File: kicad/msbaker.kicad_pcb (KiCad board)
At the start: 4 copper layers, 14 x 62 mm, 41 parts, among them J1 USB_B_Micro, J2 Micro_SD_Card, J3 GPIO, M2 MountingHole_2.2mm_M2_ISO1458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, U1 MIC5365-3.3YC5, U2 W25Q128JVS, U3 RP2040, U4 LSM6DSO32, Y1 12MHz

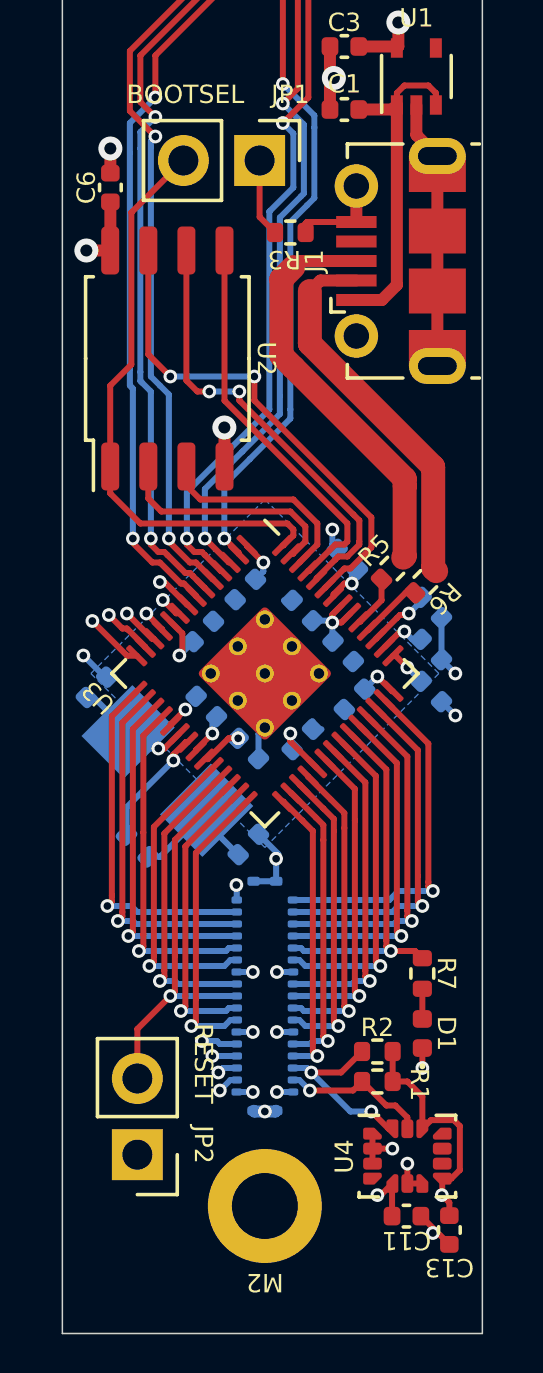
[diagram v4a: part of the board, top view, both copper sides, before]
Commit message: Added M2 screw holes to the solder paste layer to give points to align the solder paste stencil
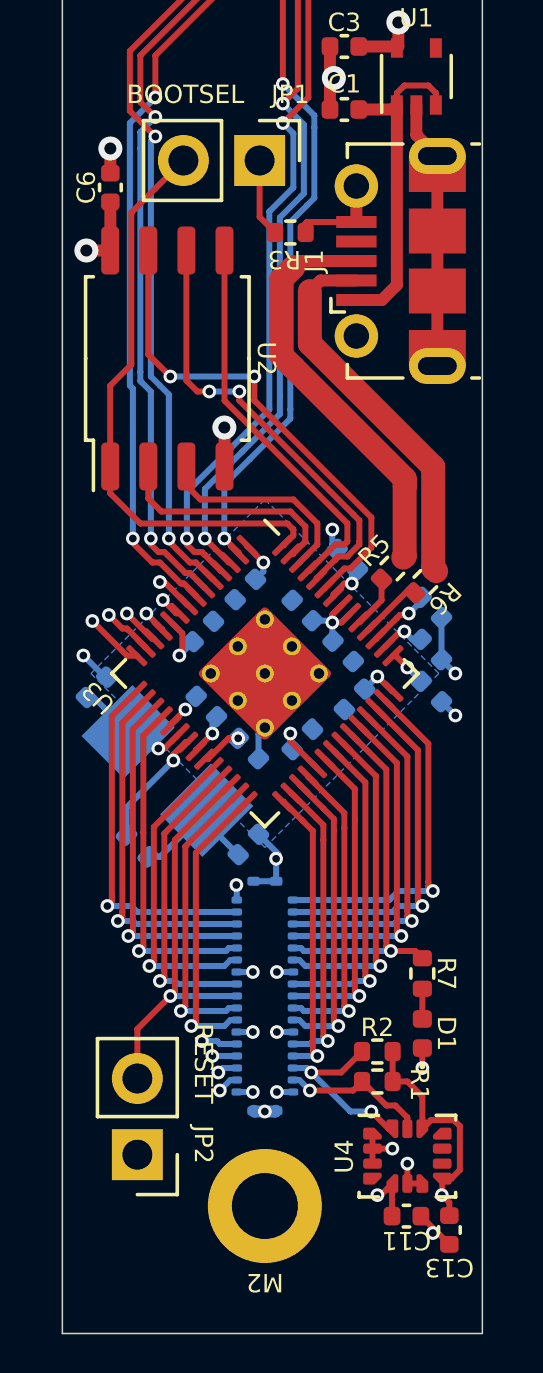
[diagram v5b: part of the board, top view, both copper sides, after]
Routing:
- net GND: track 38.5 -> 37.4 mm
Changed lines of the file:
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@@
       (outputformat 1)
       (mirror false)
-      (drillshape 1)
+      (drillshape 0)
       (scaleselection 1)
-      (outputdirectory "")
+      (outputdirectory "gerbers/")
     )
   )
@@
           ) (width 0.15) (fill yes))
       ))
-    (pad "2" smd roundrect (at -1.1625 -0.25) (size 0.625 0.4) (layers "F.Cu" "F.Paste" "F.Mask") (roundrect_rratio 0.25)
+    (pad "2" smd roundrect (at -1.1625 -0.25) (size 0.625 0.34) (layers "F.Cu" "F.Paste" "F.Mask") (roundrect_rratio 0.25)
       (net 2 "GND") (pinfunction "SDX") (pintype "bidirectional"))
-    (pad "3" smd roundrect (at -1.1625 0.25) (size 0.625 0.4) (layers "F.Cu" "F.Paste" "F.Mask") (roundrect_rratio 0.25)
+    (pad "3" smd roundrect (at -1.1625 0.25) (size 0.625 0.34) (layers "F.Cu" "F.Paste" "F.Mask") (roundrect_rratio 0.25)
       (net 2 "GND") (pinfunction "SCX") (pintype "input"))
     (pad "4" smd custom (at -1.1625 0.75) (size 0.223223 0.223223) (layers "F.Cu" "F.Paste" "F.Mask")
@@
           ) (width 0.15) (fill yes))
       ))
-    (pad "6" smd roundrect (at 0 0.9125) (size 0.4 0.625) (layers "F.Cu" "F.Paste" "F.Mask") (roundrect_rratio 0.25)
+    (pad "6" smd roundrect (at 0 0.9125) (size 0.34 0.625) (layers "F.Cu" "F.Paste" "F.Mask") (roundrect_rratio 0.25)
       (net 2 "GND") (pinfunction "GND") (pintype "power_in"))
     (pad "7" smd custom (at 0.5 0.9125) (size 0.223223 0.223223) (layers "F.Cu" "F.Paste" "F.Mask")
@@
           ) (width 0.15) (fill yes))
       ))
-    (pad "9" smd roundrect (at 1.1625 0.25) (size 0.625 0.4) (layers "F.Cu" "F.Paste" "F.Mask") (roundrect_rratio 0.25)
+    (pad "9" smd roundrect (at 1.1625 0.25) (size 0.625 0.34) (layers "F.Cu" "F.Paste" "F.Mask") (roundrect_rratio 0.25)
       (net 56 "unconnected-(U4-Pad9)") (pinfunction "INT2") (pintype "output+no_connect"))
-    (pad "10" smd roundrect (at 1.1625 -0.25) (size 0.625 0.4) (layers "F.Cu" "F.Paste" "F.Mask") (roundrect_rratio 0.25)
+    (pad "10" smd roundrect (at 1.1625 -0.25) (size 0.625 0.34) (layers "F.Cu" "F.Paste" "F.Mask") (roundrect_rratio 0.25)
       (net 57 "unconnected-(U4-Pad10)") (pinfunction "NC") (pintype "no_connect"))
     (pad "11" smd custom (at 1.1625 -0.75) (size 0.223223 0.223223) (layers "F.Cu" "F.Paste" "F.Mask")
@@
           ) (width 0.15) (fill yes))
       ))
-    (pad "13" smd roundrect (at 0 -0.9125) (size 0.4 0.625) (layers "F.Cu" "F.Paste" "F.Mask") (roundrect_rratio 0.25)
+    (pad "13" smd roundrect (at 0 -0.9125) (size 0.34 0.625) (layers "F.Cu" "F.Paste" "F.Mask") (roundrect_rratio 0.25)
       (net 42 "/I2C0_SCL") (pinfunction "SCL") (pintype "input"))
     (pad "14" smd custom (at -0.5 -0.9125) (size 0.223223 0.223223) (layers "F.Cu" "F.Paste" "F.Mask")
@@
     (fp_line (start -3.5 3.5) (end -3.5 -2.5) (layer "F.Fab") (width 0.1))
     (fp_line (start 3.5 3.5) (end -3.5 3.5) (layer "F.Fab") (width 0.1))
-    (pad "" smd roundrect (at -0.6375 0.6375 315) (size 1.084435 1.084435) (layers "F.Paste") (roundrect_rratio 0.230535))
-    (pad "" smd roundrect (at 0.6375 0.6375 315) (size 1.084435 1.084435) (layers "F.Paste") (roundrect_rratio 0.230535))
-    (pad "" smd roundrect (at -0.6375 -0.6375 315) (size 1.084435 1.084435) (layers "F.Paste") (roundrect_rratio 0.230535))
-    (pad "" smd roundrect (at 0.6375 -0.6375 315) (size 1.084435 1.084435) (layers "F.Paste") (roundrect_rratio 0.230535))
+    (pad "" smd roundrect (at -0.6375 0.6375 315) (size 1.084435 1.084435) (layers "F.Paste") (roundrect_rratio 0.2305347946))
+    (pad "" smd roundrect (at 0.6375 0.6375 315) (size 1.084435 1.084435) (layers "F.Paste") (roundrect_rratio 0.2305347946))
+    (pad "" smd roundrect (at -0.6375 -0.6375 315) (size 1.084435 1.084435) (layers "F.Paste") (roundrect_rratio 0.2305347946))
+    (pad "" smd roundrect (at 0.6375 -0.6375 315) (size 1.084435 1.084435) (layers "F.Paste") (roundrect_rratio 0.2305347946))
     (pad "1" smd roundrect (at -3.4375 -2.6 315) (size 0.875 0.2) (layers "F.Cu" "F.Paste" "F.Mask") (roundrect_rratio 0.25)
       (net 3 "+3.3V") (pinfunction "IOVDD") (pintype "power_in"))
@@
     (property "Sheetname" "")
     (attr smd)
-    (fp_text reference "C18" (at 0.02038 -0.813173 -135 unlocked) (layer "B.SilkS")
+    (fp_text reference "C18" (at 0.091091 -0.813173 -135 unlocked) (layer "B.SilkS")
       (effects (font (size 0.61 0.61) (thickness 0.0762)) (justify mirror))
     )
@@
     )
   )
+  (gr_circle (center 180.25 83) (end 181.35 83) (layer "B.Paste") (width 0) (fill solid))
+  (gr_circle (center 184.25 125.25) (end 185.35 125.25) (layer "B.Paste") (width 0) (fill solid))
+  (gr_circle (center 188.75 83) (end 189.85 83) (layer "B.Paste") (width 0) (fill solid))
+  (gr_circle (center 184.25 125.25) (end 185.35 125.25) (layer "F.Paste") (width 0) (fill solid))
+  (gr_circle (center 180.25 83) (end 181.35 83) (layer "F.Paste") (width 0) (fill solid))
+  (gr_circle (center 188.75 83) (end 189.85 83) (layer "F.Paste") (width 0) (fill solid))
   (gr_rect (start 177.5 67.5) (end 191.5 129.5) (layer "Edge.Cuts") (width 0.05) (fill none))
   (segment (start 188.65 88.55) (end 188.65 88.15) (width 0.2) (layer "F.Cu") (net 1))
@@
   (segment (start 181.112214 109.187786) (end 181.6 108.7) (width 0.2) (layer "F.Cu") (net 2))
   (segment (start 182.905 100.6) (end 182.905 99.305) (width 0.4) (layer "F.Cu") (net 2))
-  (segment (start 187.24 91.31) (end 187.3 91.25) (width 0.4) (layer "F.Cu") (net 2))
   (segment (start 189.3 89.55) (end 190 90.25) (width 0.4) (layer "F.Cu") (net 2))
   (segment (start 179.1 90.82) (end 179.1 90) (width 0.4) (layer "F.Cu") (net 2))
@@
   (via (at 184.25 122.1) (size 0.457) (drill 0.254) (layers "F.Cu" "B.Cu") (net 2))
   (segment (start 186.660589 103.360589) (end 186.5 103.2) (width 0.2) (layer "B.Cu") (net 2))
-  (segment (start 184.25 109.45) (end 184.25 109.303122) (width 0.2) (layer "B.Cu") (net 2))
   (segment (start 184.039411 110.339411) (end 184.039411 109.513711) (width 0.2) (layer "B.Cu") (net 2))
   (segment (start 184.039411 112.860589) (end 184.7 113.521178) (width 0.2) (layer "B.Cu") (net 2))
@@
   (segment (start 186.55 70.25) (end 186.9 69.9) (width 0.4) (layer "B.Cu") (net 2))
   (segment (start 184.039411 109.513711) (end 184.25 109.303122) (width 0.2) (layer "B.Cu") (net 2))
-  (segment (start 183.260589 105.039411) (end 183.2 105.1) (width 0.2) (layer "B.Cu") (net 2))
   (segment (start 183.3125 121.45) (end 183.85 121.45) (width 0.2) (layer "B.Cu") (net 2))
   (segment (start 184.625 113.675) (end 184.7 113.6) (width 0.2) (layer "B.Cu") (net 2))
@@
   (segment (start 186.5 103.2) (end 186.5 102.7) (width 0.2) (layer "B.Cu") (net 2))
   (segment (start 183.3125 119.45) (end 183.85 119.45) (width 0.2) (layer "B.Cu") (net 2))
-  (segment (start 185.160589 105.060589) (end 184.886289 105.060589) (width 0.2) (layer "B.Cu") (net 2))
   (segment (start 184.625 114.425) (end 184.625 113.675) (width 0.2) (layer "B.Cu") (net 2))
   (segment (start 178.921178 107.621178) (end 178.2 106.9) (width 0.2) (layer "B.Cu") (net 2))
   (segment (start 183.875 114.425) (end 184.625 114.425) (width 0.2) (layer "B.Cu") (net 2))
   (segment (start 183.9 122.1) (end 184.25 122.1) (width 0.4) (layer "B.Cu") (net 2))
-  (segment (start 185.839411 109.360589) (end 186.139411 109.360589) (width 0.2) (layer "B.Cu") (net 2))
   (segment (start 183.3125 117.45) (end 183.85 117.45) (width 0.2) (layer "B.Cu") (net 2))
   (segment (start 184.7 113.521178) (end 184.7 113.6) (width 0.2) (layer "B.Cu") (net 2))
-  (segment (start 183.198439 108.401561) (end 183.348439 108.401561) (width 0.2) (layer "B.Cu") (net 2))
-  (segment (start 183.348439 106.569617) (end 183.348439 106.598439) (width 0.2) (layer "B.Cu") (net 2))
   (segment (start 185.1875 121.45) (end 184.65 121.45) (width 0.2) (layer "B.Cu") (net 2))
   (segment (start 184.6 122.1) (end 184.625 122.075) (width 0.4) (layer "B.Cu") (net 2))
@@
   (segment (start 185.839411 109.360589) (end 185.839411 109.089411) (width 0.2) (layer "B.Cu") (net 2))
   (segment (start 185.1875 119.45) (end 184.65 119.45) (width 0.2) (layer "B.Cu") (net 2))
-  (segment (start 186.7 103.321178) (end 186.660589 103.360589) (width 0.2) (layer "B.Cu") (net 2))
   (segment (start 185.1875 117.45) (end 184.65 117.45) (width 0.2) (layer "B.Cu") (net 2))
   (segment (start 186.5 105.8) (end 186.798529 105.8) (width 0.2) (layer "F.Cu") (net 3))
@@
   (segment (start 185.1 109.978822) (end 185.1 109.5) (width 0.2) (layer "B.Cu") (net 3))
   (segment (start 183.939411 104.360589) (end 184.2 104.1) (width 0.2) (layer "B.Cu") (net 3))
-  (segment (start 186.460589 106.360589) (end 186.6 106.221178) (width 0.2) (layer "B.Cu") (net 3))
   (segment (start 186.439411 105.739411) (end 186.5 105.8) (width 0.2) (layer "B.Cu") (net 3))
   (segment (start 183.3125 114.5625) (end 183.3 114.55) (width 0.2) (layer "B.Cu") (net 3))
@@
   (segment (start 189.460589 105.089411) (end 189.460589 104.960589) (width 0.2) (layer "B.Cu") (net 6))
   (segment (start 187.15 104.5) (end 187.15 104.228822) (width 0.2) (layer "B.Cu") (net 6))
-  (segment (start 187.4 104.1) (end 187.339411 104.039411) (width 0.2) (layer "B.Cu") (net 6))
   (segment (start 187.15 104.228822) (end 187.339411 104.039411) (width 0.2) (layer "B.Cu") (net 6))
   (segment (start 189.5 118.01) (end 189.5 119.015) (width 0.2) (layer "F.Cu") (net 7))
@@
   (segment (start 183.3125 120.25) (end 182.5 120.25) (width 0.2) (layer "B.Cu") (net 39))
   (segment (start 188.375 122.675) (end 188.5 122.675) (width 0.2) (layer "F.Cu") (net 40))
-  (segment (start 181.677899 105.210742) (end 181.677899 105.177899) (width 0.1524) (layer "F.Cu") (net 40))
   (segment (start 181.15 104.7) (end 180.9 104.45) (width 0.2) (layer "F.Cu") (net 40))
   (segment (start 185.8 120.8) (end 186.79 120.8) (width 0.2) (layer "F.Cu") (net 40))

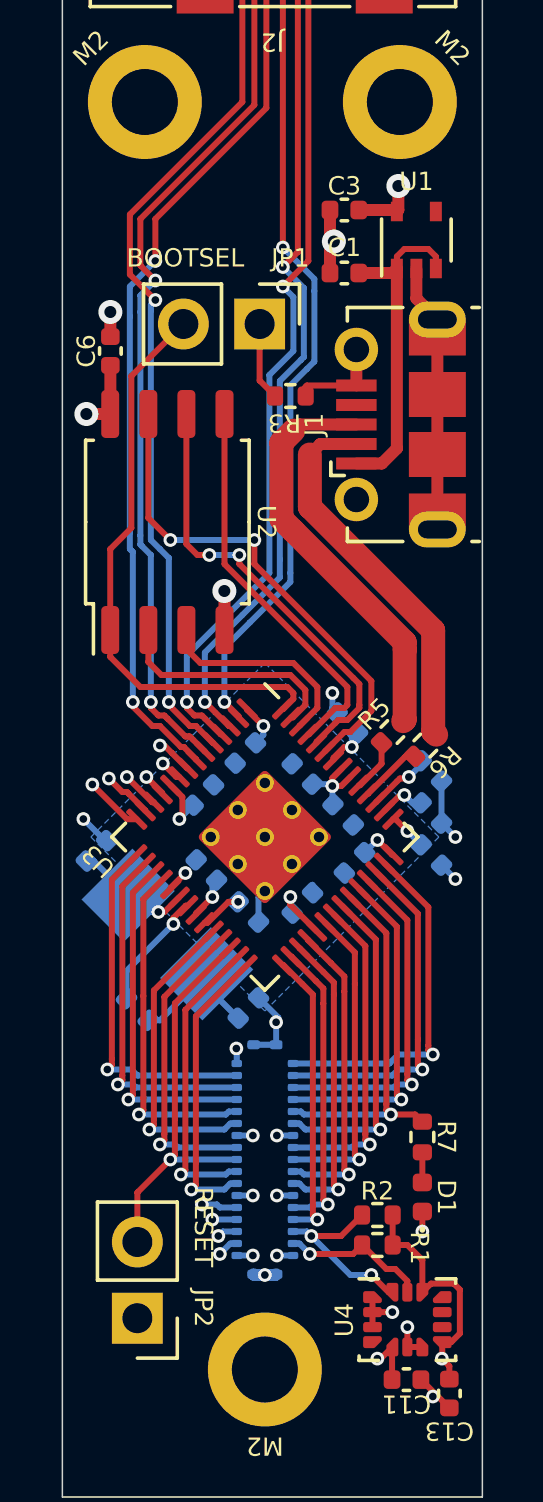
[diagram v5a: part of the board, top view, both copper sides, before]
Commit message: Added test points to schematic
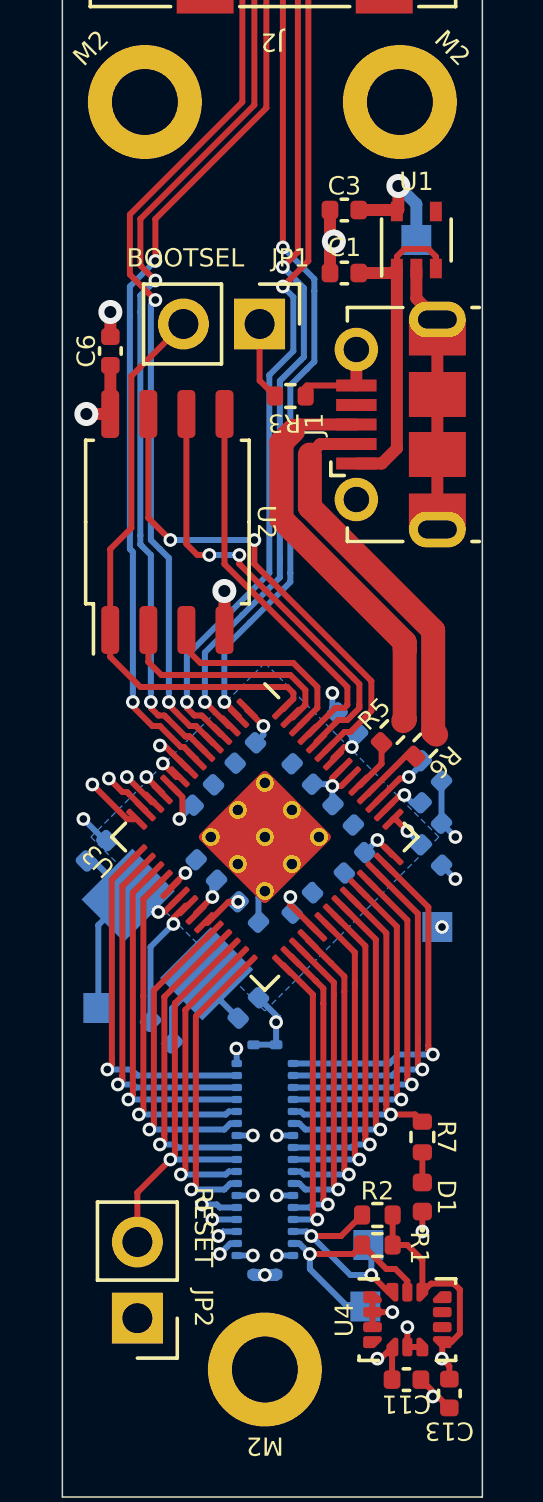
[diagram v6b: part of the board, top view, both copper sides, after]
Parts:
- added TP1: +1.1v Supply, TestPoint:TestPoint_Pad_1.0x1.0mm, B.Cu at (190.0, 110.5)
- added TP2: +3.3v Supply, TestPoint:TestPoint_Pad_1.0x1.0mm, B.Cu at (189.3, 87.6)
- added TP3: XIN, TestPoint:TestPoint_Pad_1.0x1.0mm, B.Cu at (178.7, 113.2)
- added TP4: I2C SDA, TestPoint:TestPoint_Pad_1.0x1.0mm, B.Cu at (187.7, 121.1)
- added TP5: I2C SCL, TestPoint:TestPoint_Pad_1.0x1.0mm, B.Cu at (187.6, 123.2)
- R7: value 120 -> 480
- moved R4 1.10 mm to (180.8, 114.0)
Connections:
- net Net-(C4-Pad2) renamed /XIN
- net Net-(C7-Pad1) renamed +1V1
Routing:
- net /XIN: track 4.00 -> 8.17 mm
- net /I2C0_SCL: track 24.3 -> 27.4 mm
- net +1V1: track 17.1 -> 19.8 mm, vias 3 -> 4
- net +3.3V: track 31.4 -> 33.4 mm
- net /I2C0_SDA: track 26.3 -> 27.3 mm

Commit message: Updated to v3
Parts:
- added G***: LOGO, msbaker:openapeshop, F.Cu at (148.8, 122.5)
- added G***: LOGO, msbaker:qrcode, B.Cu at (148.5, 83.2)
- moved C13 36.6 mm to (154.4, 132.6)
- moved C1 36.6 mm to (150.9, 95.2)
- moved C10 36.6 mm to (153.8, 114.6)
- moved C11 36.6 mm to (153.0, 132.1)
- moved C12 36.6 mm to (150.9, 113.3)
- moved C14 36.6 mm to (147.6, 111.2)
- moved C15 36.6 mm to (146.2, 112.6)
- moved C16 36.6 mm to (146.3, 115.1)
- moved C17 36.6 mm to (149.5, 116.2)
- moved C18 36.6 mm to (151.2, 114.9)
- moved C19 36.6 mm to (149.5, 111.9)
- moved C2 36.6 mm to (149.8, 77.4)
- moved C20 36.6 mm to (153.8, 113.2)
- moved C3 36.6 mm to (150.9, 93.1)
- moved C4 36.6 mm to (142.6, 114.5)
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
